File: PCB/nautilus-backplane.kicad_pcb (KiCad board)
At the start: 4 copper layers, 130.2 x 60.1 mm, 97 parts, among them J1 DE9_Socket_MountingHoles, J18 615008138321, J2 24.245.2, J3 24.245.2, J4 24.245.2, J5 24.245.2, J8 EdgeConn_Full, J9 643280100305

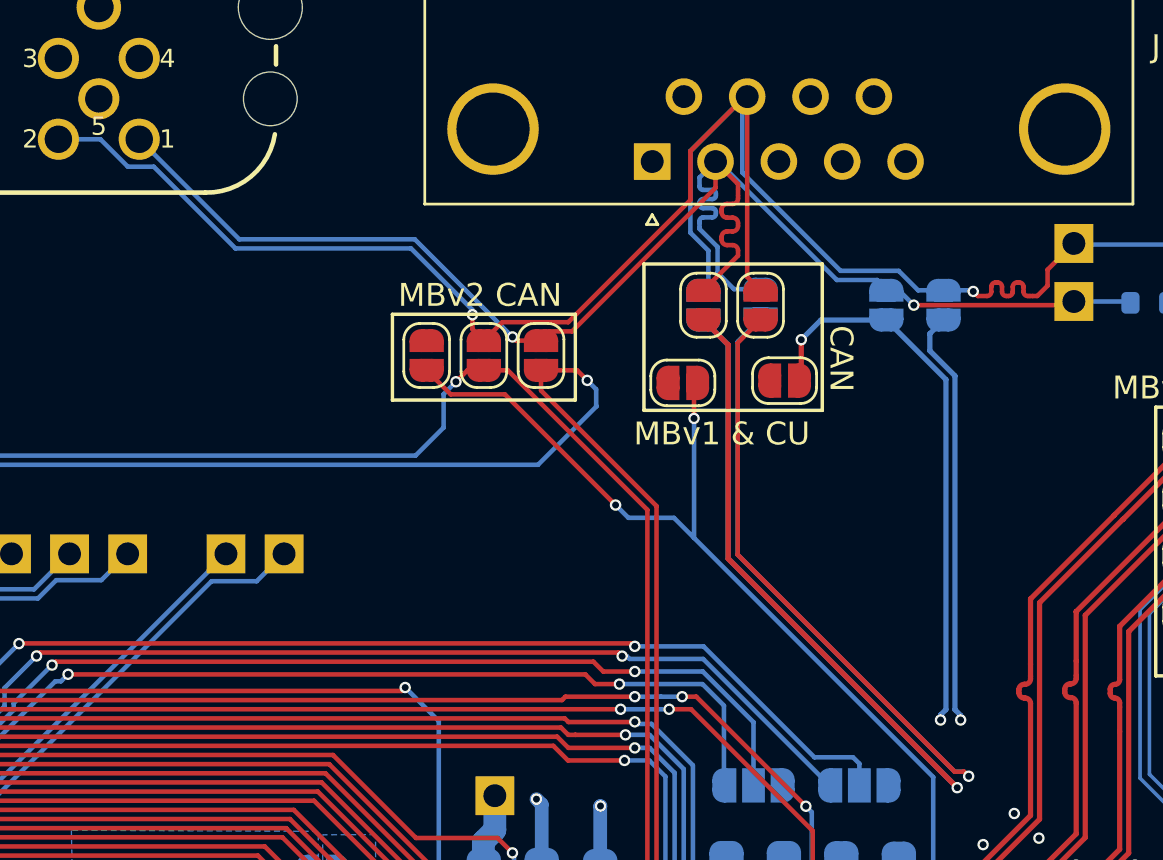
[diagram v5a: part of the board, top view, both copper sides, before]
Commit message: tuned CAN lines
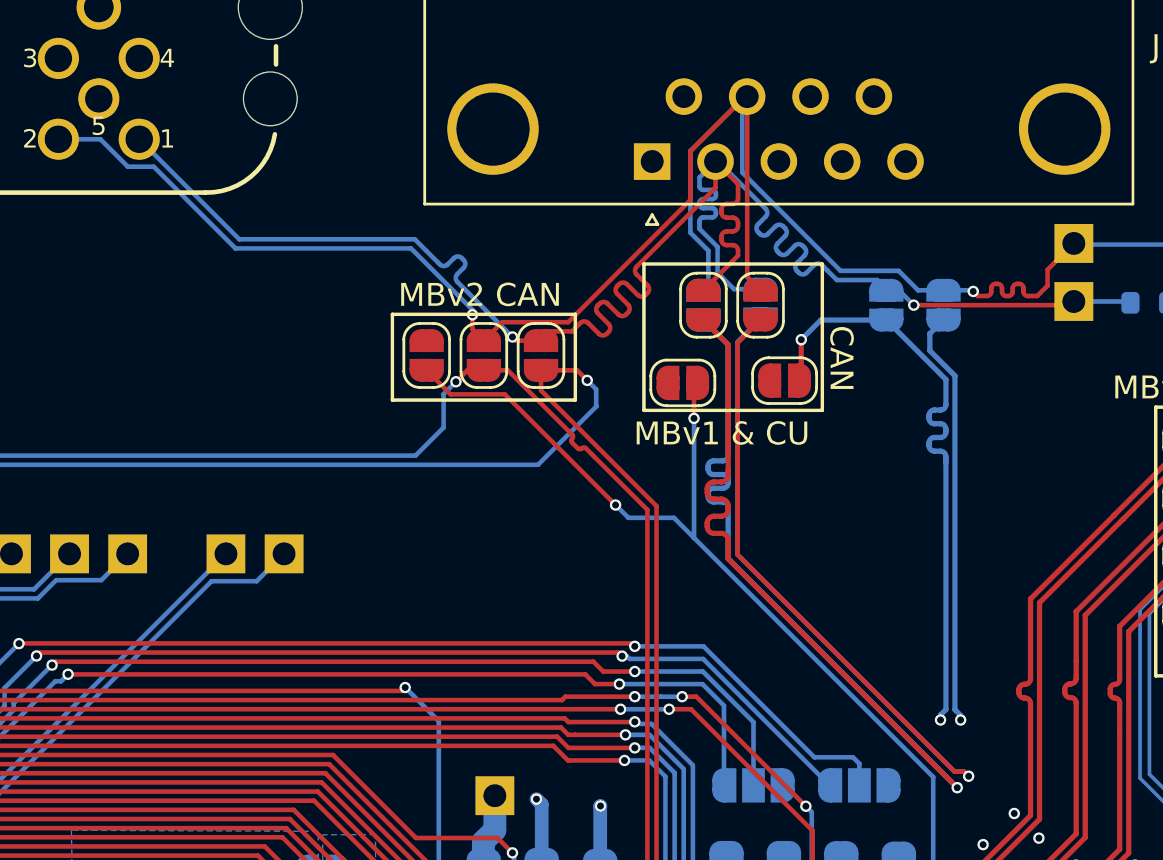
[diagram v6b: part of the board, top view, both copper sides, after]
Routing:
- net /FISH/CAN.L: track 72.2 -> 83.4 mm
- net e2_1-: track 107.0 -> 112.2 mm
- net e2_1+: track 60.5 -> 62.6 mm
